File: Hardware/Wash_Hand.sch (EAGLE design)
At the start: 65 parts, among them IC1 LM358D, IC2 LP298XS, IC3 405016TSSOP, J1 I2C, J2 ICSP, J3 SPI, J4 9V_CONN, J5 EXT_VCC, J6 6_PIN_SERIAL_CABLEPTH, Q1 16.0 Mhz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

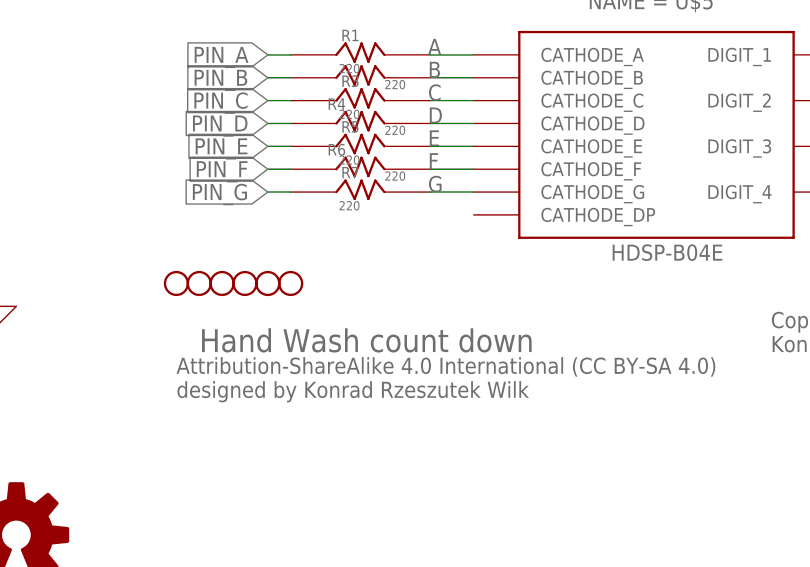
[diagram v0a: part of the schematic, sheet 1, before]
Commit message: Schematic/Board: Add fiducial
Signed-off-by: Konrad Rzeszutek Wilk <konrad@kernel.org>
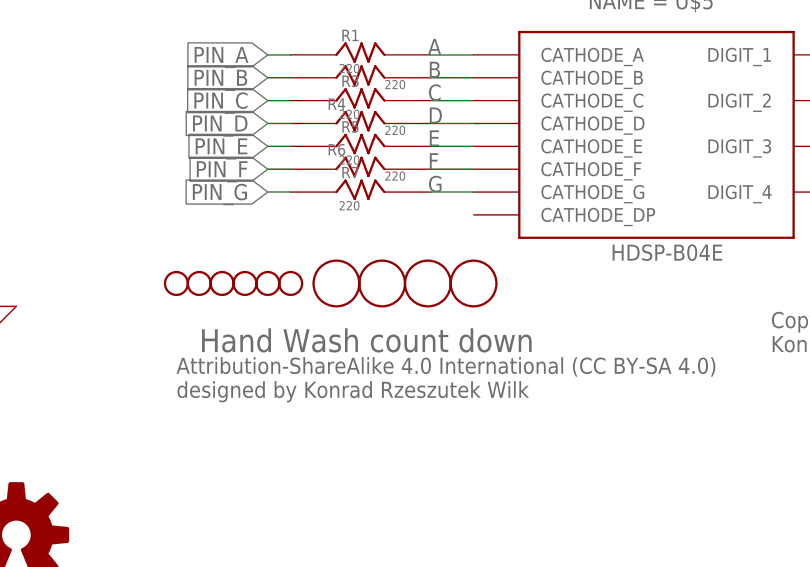
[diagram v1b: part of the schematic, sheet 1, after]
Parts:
- added U$10, U$7, U$8, U$9: FIDUCIAL, adafruit:FIDUCIAL
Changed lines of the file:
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@@
 <part name="Y1" library="darnok_common" deviceset="RESONATOR" device="MU" value="16MHZ"/>
 <part name="X_29" library="ngspice-simulation" library_urn="urn:adsk.eagle:library:527439" deviceset="GND" device=""/>
+<part name="U$7" library="adafruit" library_urn="urn:adsk.eagle:library:420" deviceset="FIDUCIAL" device="" package3d_urn="urn:adsk.eagle:package:6240632/1"/>
+<part name="U$8" library="adafruit" library_urn="urn:adsk.eagle:library:420" deviceset="FIDUCIAL" device="" package3d_urn="urn:adsk.eagle:package:6240632/1"/>
+<part name="U$9" library="adafruit" library_urn="urn:adsk.eagle:library:420" deviceset="FIDUCIAL" device="" package3d_urn="urn:adsk.eagle:package:6240632/1"/>
+<part name="U$10" library="adafruit" library_urn="urn:adsk.eagle:library:420" deviceset="FIDUCIAL" device="" package3d_urn="urn:adsk.eagle:package:6240632/1"/>
 </parts>
 <sheets>
@@
 </instance>
 <instance part="X_29" gate="G$1" x="17.78" y="144.78" smashed="yes" rot="R270"/>
+<instance part="U$7" gate="G$1" x="175.26" y="60.96" smashed="yes"/>
+<instance part="U$8" gate="G$1" x="180.34" y="60.96" smashed="yes"/>
+<instance part="U$9" gate="G$1" x="185.42" y="60.96" smashed="yes"/>
+<instance part="U$10" gate="G$1" x="190.5" y="60.96" smashed="yes"/>
 </instances>
 <busses>

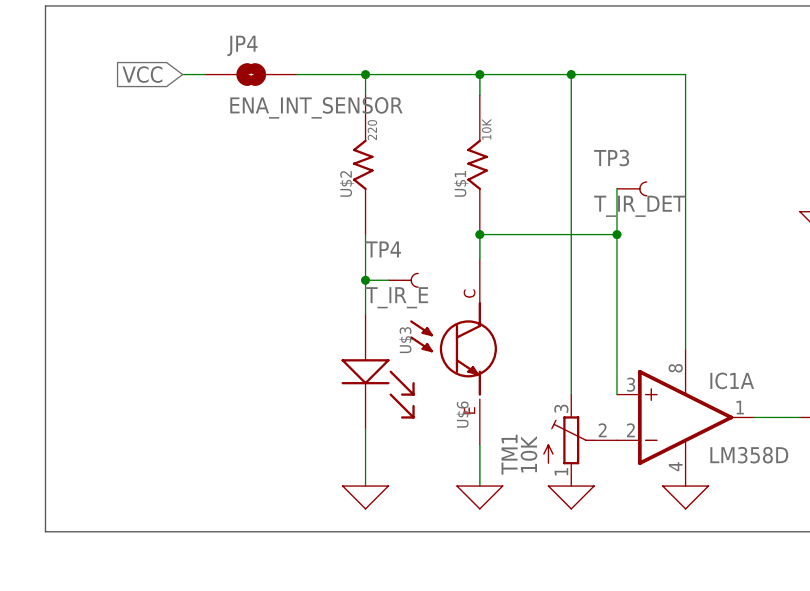
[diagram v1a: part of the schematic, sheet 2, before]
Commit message: Board/Schematic: Name some of the line sensor
circuits parts, instead of U$1,U$2, and so on.

Signed-off-by: Konrad Rzeszutek Wilk <konrad@kernel.org>
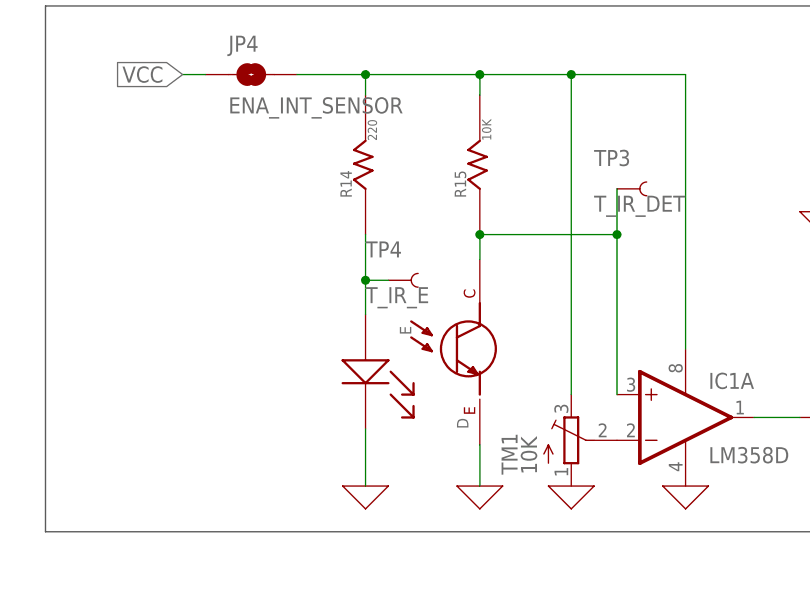
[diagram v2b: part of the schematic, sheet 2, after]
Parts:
- renumbered U$1 to R15, U$2 to R14, U$3 to E, U$6 to D
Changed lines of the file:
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@@
 <part name="JP3" library="SparkFun-Jumpers" library_urn="urn:adsk.eagle:library:528" deviceset="JUMPER-SMT_2_NO" device="_NO-SILK_ROUND" package3d_urn="urn:adsk.eagle:package:39278/1" value="ENA_INT_D0"/>
 <part name="JP4" library="SparkFun-Jumpers" library_urn="urn:adsk.eagle:library:528" deviceset="JUMPER-SMT_2_NO" device="_NO-SILK_ROUND" package3d_urn="urn:adsk.eagle:package:39278/1" value="ENA_INT_SENSOR"/>
-<part name="U$1" library="darnok_common" deviceset="RESISTOR" device="R1206" value="10K"/>
+<part name="R15" library="darnok_common" deviceset="RESISTOR" device="R1206" value="10K"/>
 <part name="X_14" library="ngspice-simulation" library_urn="urn:adsk.eagle:library:527439" deviceset="GND" device=""/>
 <part name="X_15" library="ngspice-simulation" library_urn="urn:adsk.eagle:library:527439" deviceset="GND" device=""/>
 <part name="IC1" library="linear" library_urn="urn:adsk.eagle:library:262" deviceset="LM358" device="D" package3d_urn="urn:adsk.eagle:package:16404/2"/>
 <part name="TM1" library="adafruit" library_urn="urn:adsk.eagle:library:420" deviceset="TRIMPOT" device="TC33X" package3d_urn="urn:adsk.eagle:package:6240639/1" value="10K"/>
-<part name="U$3" library="darnok_sensors" deviceset="LTE-302" device=""/>
-<part name="U$6" library="darnok_sensors" deviceset="LTR-301" device=""/>
+<part name="E" library="darnok_sensors" deviceset="LTE-302" device=""/>
+<part name="D" library="darnok_sensors" deviceset="LTR-301" device=""/>
 <part name="X_16" library="ngspice-simulation" library_urn="urn:adsk.eagle:library:527439" deviceset="GND" device=""/>
-<part name="U$2" library="darnok_common" deviceset="RESISTOR" device="R1206" value="220"/>
+<part name="R14" library="darnok_common" deviceset="RESISTOR" device="R1206" value="220"/>
 <part name="FRAME2" library="frames" library_urn="urn:adsk.eagle:library:229" deviceset="LETTER_L" device="">
 <attribute name="REVISION" value="v1.3b.rc4"/>
@@
 <attribute name="VALUE" x="139.7" y="167.64" size="1.778" layer="96" font="vector" align="top-left"/>
 </instance>
-<instance part="U$1" gate="G$1" x="167.64" y="157.48" smashed="yes" rot="R90">
+<instance part="R15" gate="G$1" x="167.64" y="157.48" smashed="yes" rot="R90">
 <attribute name="NAME" x="166.116" y="156.464" size="1.27" layer="95" rot="R90"/>
 <attribute name="VALUE" x="168.91" y="162.814" size="1.016" layer="96" rot="R90"/>
@@
 <attribute name="VALUE" x="173.99" y="125.73" size="1.778" layer="96" rot="R90"/>
 </instance>
-<instance part="U$3" gate="G$1" x="154.94" y="137.16" smashed="yes" rot="R270">
+<instance part="E" gate="G$1" x="154.94" y="137.16" smashed="yes" rot="R270">
 <attribute name="NAME" x="158.75" y="142.24" size="1.27" layer="95" rot="R270"/>
 </instance>
-<instance part="U$6" gate="G$1" x="167.64" y="139.7" smashed="yes" rot="R90">
+<instance part="D" gate="G$1" x="167.64" y="139.7" smashed="yes" rot="R90">
 <attribute name="NAME" x="166.37" y="130.81" size="1.27" layer="95" rot="R90"/>
 </instance>
 <instance part="X_16" gate="G$1" x="177.8" y="124.46" smashed="yes"/>
-<instance part="U$2" gate="G$1" x="154.94" y="157.48" smashed="yes" rot="R90">
+<instance part="R14" gate="G$1" x="154.94" y="157.48" smashed="yes" rot="R90">
 <attribute name="NAME" x="153.416" y="156.464" size="1.27" layer="95" rot="R90"/>
 <attribute name="VALUE" x="156.21" y="162.814" size="1.016" layer="96" rot="R90"/>
@@
 <segment>
 <pinref part="X_14" gate="G$1" pin="0"/>
-<pinref part="U$3" gate="G$1" pin="K$1"/>
+<pinref part="E" gate="G$1" pin="K$1"/>
 <wire x1="154.94" y1="124.46" x2="154.94" y2="130.81" width="0.1524" layer="91"/>
 </segment>
 <segment>
-<pinref part="U$6" gate="G$1" pin="E$1"/>
+<pinref part="D" gate="G$1" pin="E$1"/>
 <pinref part="X_15" gate="G$1" pin="0"/>
 <wire x1="167.64" y1="129.032" x2="167.64" y2="124.46" width="0.1524" layer="91"/>
@@
 <segment>
 <pinref part="JP4" gate="G$1" pin="2"/>
-<pinref part="U$1" gate="G$1" pin="R_2"/>
+<pinref part="R15" gate="G$1" pin="R_2"/>
 <wire x1="147.32" y1="170.18" x2="154.94" y2="170.18" width="0.1524" layer="91"/>
 <wire x1="154.94" y1="170.18" x2="167.64" y2="170.18" width="0.1524" layer="91"/>
@@
 <wire x1="177.8" y1="170.18" x2="167.64" y2="170.18" width="0.1524" layer="91"/>
 <junction x="167.64" y="170.18"/>
-<pinref part="U$2" gate="G$1" pin="R_2"/>
+<pinref part="R14" gate="G$1" pin="R_2"/>
 <wire x1="154.94" y1="167.894" x2="154.94" y2="170.18" width="0.1524" layer="91"/>
 <junction x="154.94" y="170.18"/>
@@
 <wire x1="182.88" y1="152.4" x2="182.88" y2="134.62" width="0.1524" layer="91"/>
 <pinref part="IC1" gate="A" pin="+IN"/>
-<pinref part="U$6" gate="G$1" pin="C$1"/>
-<pinref part="U$1" gate="G$1" pin="R_1"/>
+<pinref part="D" gate="G$1" pin="C$1"/>
+<pinref part="R15" gate="G$1" pin="R_1"/>
 <wire x1="167.64" y1="149.606" x2="167.64" y2="152.4" width="0.1524" layer="91"/>
 <wire x1="182.88" y1="152.4" x2="167.64" y2="152.4" width="0.1524" layer="91"/>
@@
 <net name="N$11" class="0">
 <segment>
-<pinref part="U$2" gate="G$1" pin="R_1"/>
+<pinref part="R14" gate="G$1" pin="R_1"/>
 <wire x1="154.94" y1="143.51" x2="154.94" y2="147.32" width="0.1524" layer="91"/>
-<pinref part="U$3" gate="G$1" pin="A$1"/>
+<pinref part="E" gate="G$1" pin="A$1"/>
 <pinref part="TP4" gate="G$1" pin="1"/>
 <wire x1="154.94" y1="147.32" x2="154.94" y2="152.4" width="0.1524" layer="91"/>

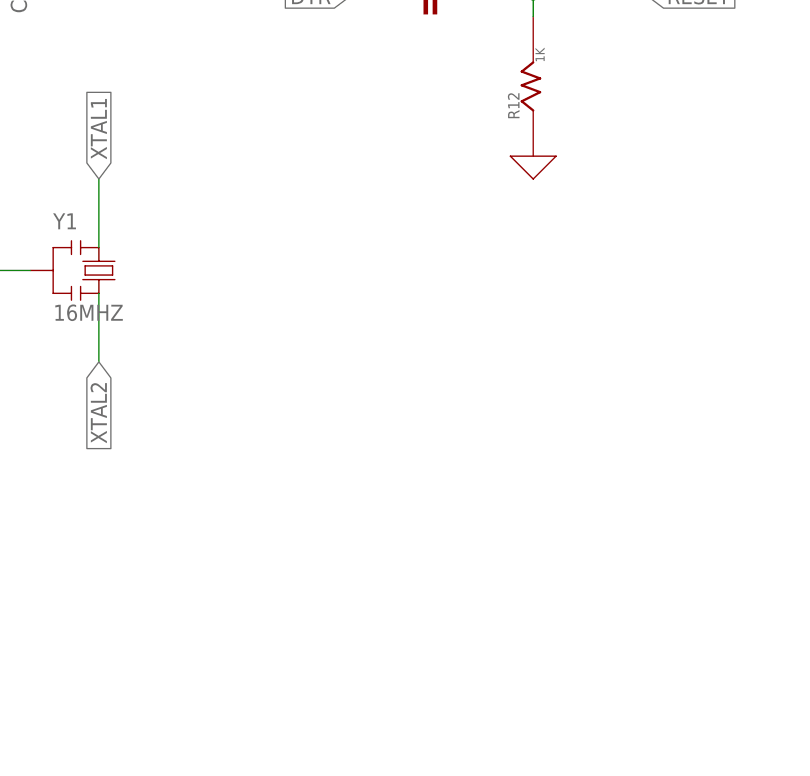
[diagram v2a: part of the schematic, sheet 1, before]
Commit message: Board/Schedule: Add 1K and LED on SCK line.
Signed-off-by: Konrad Rzeszutek Wilk <konrad@kernel.org>
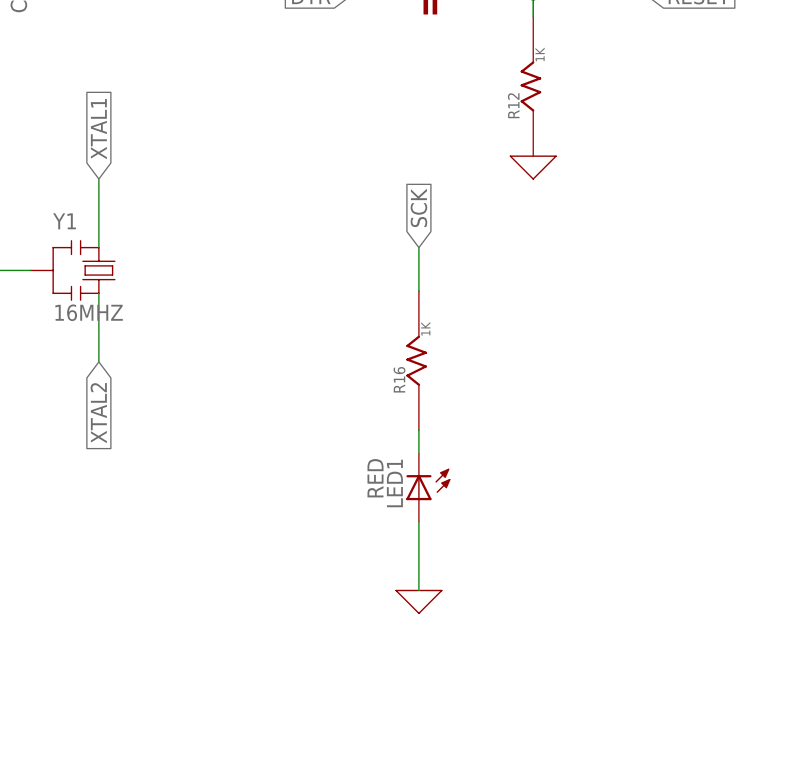
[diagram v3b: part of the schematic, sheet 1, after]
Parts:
- added LED1: RED, adafruit:LEDSMT1206
- added R16: 1K, darnok_common:RESISTORR1206
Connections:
- new net N$7: LED1.C, R16.R_1
- net 0: now also LED1.A
- net SCK: now also R16.R_2
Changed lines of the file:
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@@
 <part name="U$9" library="adafruit" library_urn="urn:adsk.eagle:library:420" deviceset="FIDUCIAL" device="" package3d_urn="urn:adsk.eagle:package:6240632/1"/>
 <part name="U$10" library="adafruit" library_urn="urn:adsk.eagle:library:420" deviceset="FIDUCIAL" device="" package3d_urn="urn:adsk.eagle:package:6240632/1"/>
+<part name="X_30" library="ngspice-simulation" library_urn="urn:adsk.eagle:library:527439" deviceset="GND" device=""/>
+<part name="LED1" library="adafruit" library_urn="urn:adsk.eagle:library:420" deviceset="LED" device="SMT1206" package3d_urn="urn:adsk.eagle:package:6240349/1" value="RED"/>
+<part name="R16" library="darnok_common" deviceset="RESISTOR" device="R1206" value="1K"/>
 </parts>
 <sheets>
@@
 <instance part="U$9" gate="G$1" x="185.42" y="60.96" smashed="yes"/>
 <instance part="U$10" gate="G$1" x="190.5" y="60.96" smashed="yes"/>
+<instance part="X_30" gate="G$1" x="66.04" y="109.22" smashed="yes"/>
+<instance part="LED1" gate="G$1" x="66.04" y="119.38" smashed="yes" rot="R180">
+<attribute name="NAME" x="62.484" y="123.952" size="1.778" layer="95" rot="R270"/>
+<attribute name="VALUE" x="60.325" y="123.952" size="1.778" layer="96" rot="R270"/>
+</instance>
+<instance part="R16" gate="G$1" x="66.04" y="132.08" smashed="yes" rot="R90">
+<attribute name="NAME" x="64.516" y="131.064" size="1.27" layer="95" rot="R90"/>
+<attribute name="VALUE" x="67.31" y="137.414" size="1.016" layer="96" rot="R90"/>
+</instance>
 </instances>
 <busses>
@@
 <pinref part="X_29" gate="G$1" pin="0"/>
 </segment>
+<segment>
+<pinref part="LED1" gate="G$1" pin="A"/>
+<pinref part="X_30" gate="G$1" pin="0"/>
+<wire x1="66.04" y1="116.84" x2="66.04" y2="109.22" width="0.1524" layer="91"/>
+</segment>
 </net>
 <net name="D0" class="0">
@@
 <label x="187.96" y="99.06" size="1.778" layer="95" xref="yes"/>
 <pinref part="U2" gate="U$1" pin="PB5(SCK)"/>
+</segment>
+<segment>
+<pinref part="R16" gate="G$1" pin="R_2"/>
+<wire x1="66.04" y1="142.494" x2="66.04" y2="147.32" width="0.1524" layer="91"/>
+<label x="66.04" y="147.32" size="1.778" layer="95" rot="R90" xref="yes"/>
 </segment>
 </net>
@@
 </segment>
 </net>
+<net name="N$7" class="0">
+<segment>
+<pinref part="R16" gate="G$1" pin="R_1"/>
+<pinref part="LED1" gate="G$1" pin="C"/>
+<wire x1="66.04" y1="127" x2="66.04" y2="124.46" width="0.1524" layer="91"/>
+</segment>
+</net>

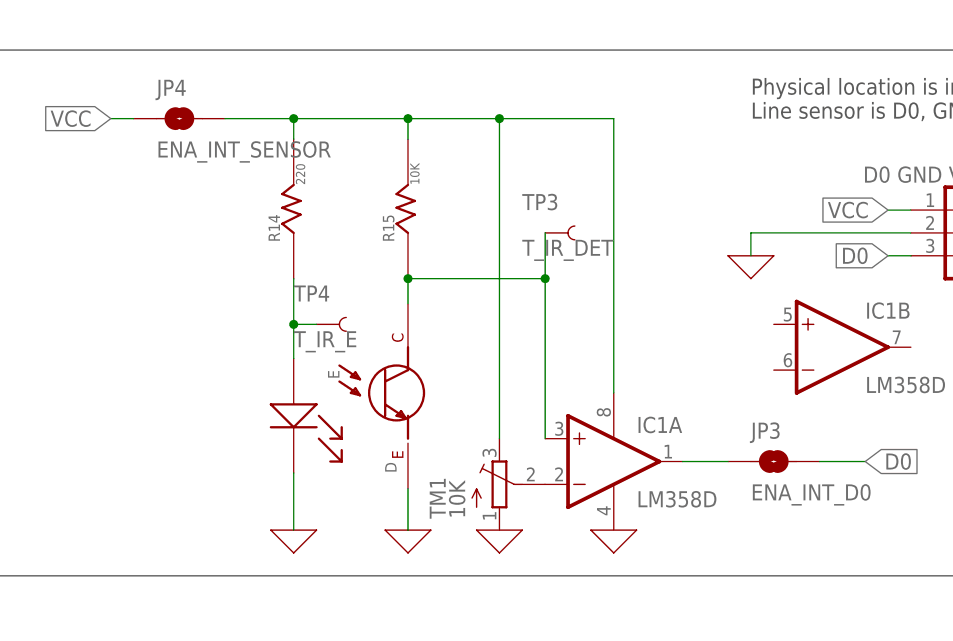
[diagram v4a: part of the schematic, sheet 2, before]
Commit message: Board/Schematic: Replace open with closed SMT pads for line sensor
As we want it by default enabled.

Signed-off-by: Konrad Rzeszutek Wilk <konrad@kernel.org>
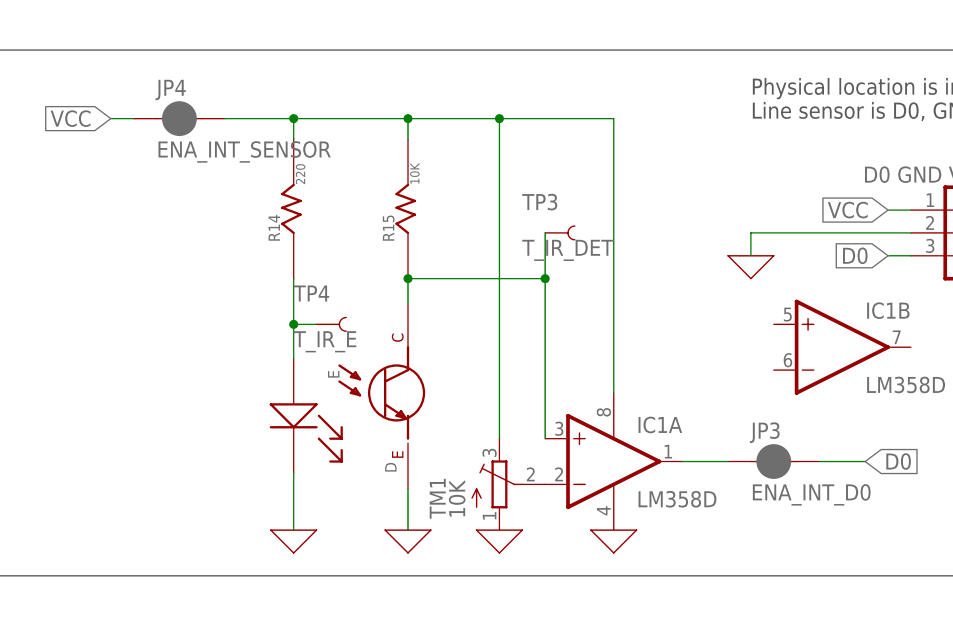
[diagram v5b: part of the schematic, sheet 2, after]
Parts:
- JP3, JP4: device SparkFun-Jumpers:JUMPER-SMT_2_NO_NO-SILK_ROUND -> SparkFun-Jumpers:JUMPER-SMT_2_NC_PASTE_SILK
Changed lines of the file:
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@@
 <part name="X_13" library="ngspice-simulation" library_urn="urn:adsk.eagle:library:527439" deviceset="GND" device=""/>
 <part name="JP2" library="SparkFun-Jumpers" library_urn="urn:adsk.eagle:library:528" deviceset="JUMPER-SMT_3_1-NC_PASTE" device="_SILK" package3d_urn="urn:adsk.eagle:package:39293/1" value="9V_JUMPER"/>
-<part name="JP3" library="SparkFun-Jumpers" library_urn="urn:adsk.eagle:library:528" deviceset="JUMPER-SMT_2_NO" device="_NO-SILK_ROUND" package3d_urn="urn:adsk.eagle:package:39278/1" value="ENA_INT_D0"/>
-<part name="JP4" library="SparkFun-Jumpers" library_urn="urn:adsk.eagle:library:528" deviceset="JUMPER-SMT_2_NO" device="_NO-SILK_ROUND" package3d_urn="urn:adsk.eagle:package:39278/1" value="ENA_INT_SENSOR"/>
+<part name="JP3" library="SparkFun-Jumpers" library_urn="urn:adsk.eagle:library:528" deviceset="JUMPER-SMT_2_NC_PASTE" device="_SILK" package3d_urn="urn:adsk.eagle:package:39282/1" value="ENA_INT_D0"/>
+<part name="JP4" library="SparkFun-Jumpers" library_urn="urn:adsk.eagle:library:528" deviceset="JUMPER-SMT_2_NC_PASTE" device="_SILK" package3d_urn="urn:adsk.eagle:package:39282/1" value="ENA_INT_SENSOR"/>
 <part name="R15" library="darnok_common" deviceset="RESISTOR" device="R1206" value="10K"/>
 <part name="X_14" library="ngspice-simulation" library_urn="urn:adsk.eagle:library:527439" deviceset="GND" device=""/>
